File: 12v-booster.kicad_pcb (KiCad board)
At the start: 2 copper layers, 21.9 x 10.3 mm, 18 parts, among them J1 Conn_01x04, J2 Conn_01x03, Q1 BSS214NW, U1 TPS55340-Q1

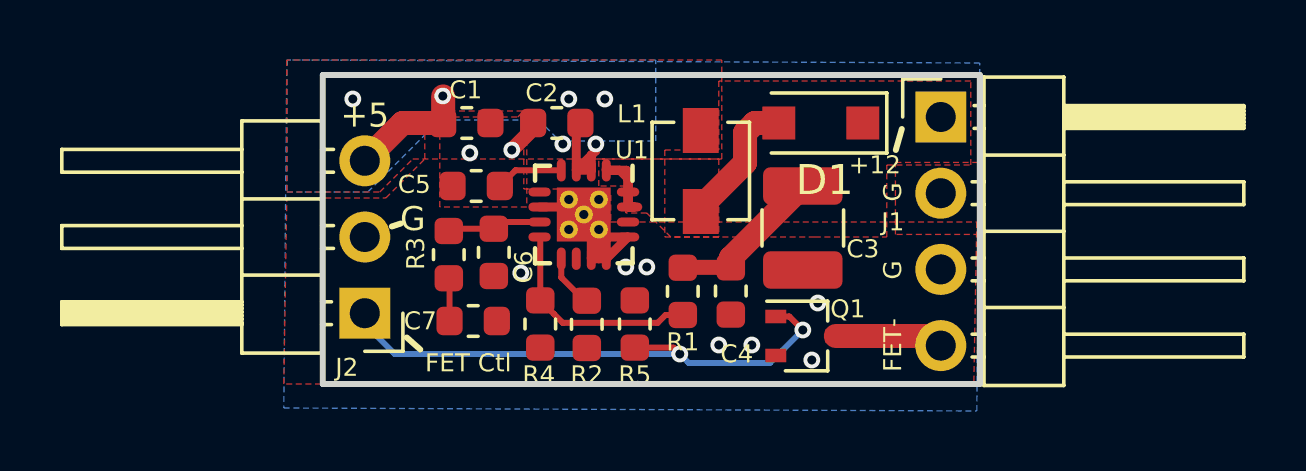
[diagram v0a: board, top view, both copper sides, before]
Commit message: Fixed solder mask clearance.
Signed-off-by: Aaron Williams <aaron.w2@gmail.com>
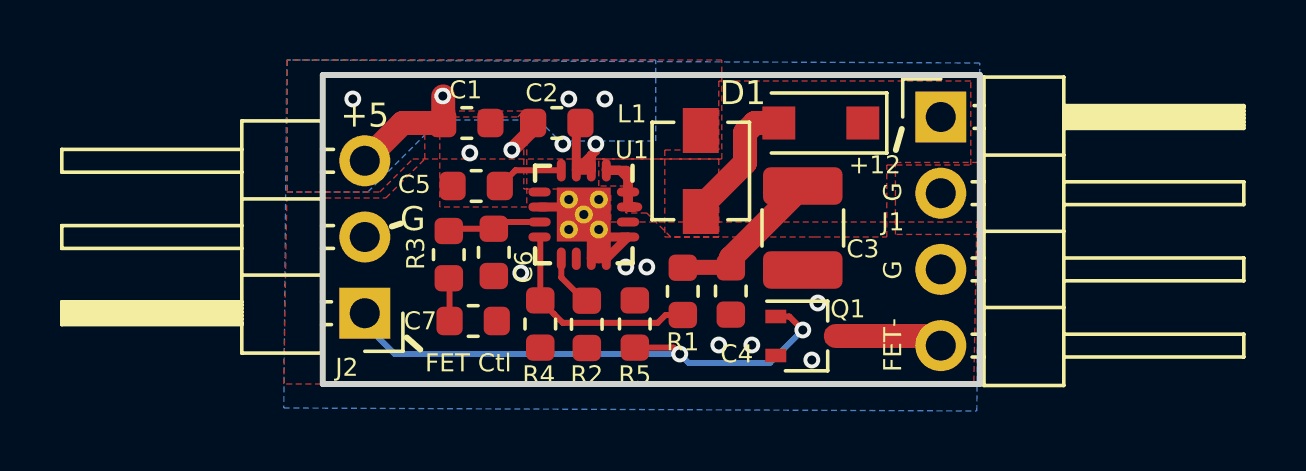
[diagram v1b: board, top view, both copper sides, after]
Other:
- rule pad_to_mask_clearance: 0.2 -> 0.0508
- rule trace_min: 0.2 -> 0.1524
- board text added: "Version 1.2"
- board text removed: "Version 1.1"
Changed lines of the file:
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@@
-(kicad_pcb (version 20171130) (host pcbnew 5.0.0)
+(kicad_pcb (version 20171130) (host pcbnew 5.0.0-5.0.0)
   (general
     (thickness 1.6)
@@
   )
   (setup
-    (last_trace_width 0.8)
+    (last_trace_width 0.2)
     (user_trace_width 0.2)
     (user_trace_width 0.3)
@@
     (zone_clearance 0.508)
     (zone_45_only yes)
-    (trace_min 0.2)
+    (trace_min 0.1524)
     (segment_width 0.2)
     (edge_width 0.1)
@@
     (pad_size 1.524 1.524)
     (pad_drill 0.762)
-    (pad_to_mask_clearance 0.2)
+    (pad_to_mask_clearance 0.0508)
     (aux_axis_origin 0 0)
     (visible_elements FFFFFF7F)
@@
     (tags D_SOD-123F)
     (attr smd)
-    (fp_text reference D1 (at -0.127 -1.905 180) (layer F.SilkS)
-      (effects (font (size 1 1) (thickness 0.15)))
+    (fp_text reference D1 (at 2.6 1 180) (layer F.SilkS)
+      (effects (font (size 0.8 0.8) (thickness 0.1)))
     )
     (fp_text value D_Schottky (at 0 2.1 180) (layer F.Fab)
@@
   )
   (gr_line (start 131.3 74) (end 131.5 73.3) (layer F.SilkS) (width 0.2))
-  (gr_text "Version 1.1" (at 125.55 74.9) (layer B.SilkS)
+  (gr_text "Version 1.2" (at 125.55 74.9) (layer B.SilkS)
     (effects (font (size 0.8 0.8) (thickness 0.1)) (justify mirror))
   )
@@
   (segment (start 119.2125 73.1) (end 119.2125 73.2875) (width 0.5) (layer F.Cu) (net 3) (status 30))
   (via (at 118.8 78.1) (size 0.56) (drill 0.3) (layers F.Cu B.Cu) (net 3))
+  (segment (start 125.575 79.25) (end 125.7 79.25) (width 0.2) (layer F.Cu) (net 3))
+  (via (at 126.5 80.5) (size 0.56) (drill 0.3) (layers F.Cu B.Cu) (net 3))
+  (via (at 125.4 80.5) (size 0.56) (drill 0.3) (layers F.Cu B.Cu) (net 3))
+  (via (at 128.7 79.1) (size 0.56) (drill 0.3) (layers F.Cu B.Cu) (net 3))
+  (via (at 128.5 81) (size 0.56) (drill 0.3) (layers F.Cu B.Cu) (net 3))
   (segment (start 120.15 78.25) (end 120.15 77.625) (width 0.2) (layer F.Cu) (net 4) (status 20))
   (segment (start 121.1 79.2) (end 120.15 78.25) (width 0.2) (layer F.Cu) (net 4) (status 10))
@@
   (segment (start 121.65 74.675) (end 122.1 74.675) (width 0.3) (layer F.Cu) (net 12) (status 10))
   (segment (start 122.375 75.9) (end 122.7 75.9) (width 0.3) (layer F.Cu) (net 12) (status 30))
+  (segment (start 126.27499 74.42501) (end 126.27499 73.42501) (width 0.8) (layer F.Cu) (net 12))
+  (segment (start 124.8 76.05) (end 124.8 75.9) (width 0.8) (layer F.Cu) (net 12))
+  (segment (start 124.8 75.9) (end 126.27499 74.42501) (width 0.8) (layer F.Cu) (net 12))
+  (segment (start 126.6 73.1) (end 127.3 73.1) (width 0.8) (layer F.Cu) (net 12))
+  (segment (start 126.27499 73.42501) (end 126.6 73.1) (width 0.8) (layer F.Cu) (net 12))
   (via (at 124.1 80.8) (size 0.56) (drill 0.3) (layers F.Cu B.Cu) (net 13))
   (segment (start 124.0875 80.7875) (end 124.1 80.8) (width 0.2) (layer F.Cu) (net 13))
@@
   (segment (start 123.8875 80.5875) (end 124.1 80.8) (width 0.2) (layer F.Cu) (net 13))
   (segment (start 122.6 80.5875) (end 123.8875 80.5875) (width 0.2) (layer F.Cu) (net 13))
-  (segment (start 125.575 79.25) (end 125.7 79.25) (width 0.2) (layer F.Cu) (net 3))
-  (via (at 126.5 80.5) (size 0.56) (drill 0.3) (layers F.Cu B.Cu) (net 3))
-  (via (at 125.4 80.5) (size 0.56) (drill 0.3) (layers F.Cu B.Cu) (net 3))
-  (via (at 128.7 79.1) (size 0.56) (drill 0.3) (layers F.Cu B.Cu) (net 3))
-  (via (at 128.5 81) (size 0.56) (drill 0.3) (layers F.Cu B.Cu) (net 3))
-  (segment (start 126.27499 74.42501) (end 126.27499 73.42501) (width 0.8) (layer F.Cu) (net 12))
-  (segment (start 124.8 76.05) (end 124.8 75.9) (width 0.8) (layer F.Cu) (net 12))
-  (segment (start 124.8 75.9) (end 126.27499 74.42501) (width 0.8) (layer F.Cu) (net 12))
-  (segment (start 126.6 73.1) (end 127.3 73.1) (width 0.8) (layer F.Cu) (net 12))
-  (segment (start 126.27499 73.42501) (end 126.6 73.1) (width 0.8) (layer F.Cu) (net 12))
   (via (at 128.2 80) (size 0.56) (drill 0.3) (layers F.Cu B.Cu) (net 13))
   (segment (start 127.3 79.55) (end 127.75 79.55) (width 0.2) (layer F.Cu) (net 13))
